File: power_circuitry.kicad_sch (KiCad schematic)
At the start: 32 parts, among them U1 ACS723xLCTR-10AU, U2 ACS723xLCTR-10AU, U3 MCP6007, U4 MCP6007, U5 MCP6007, U6 ACS723xLCTR-10AU, U7 MCP6007, U8 MCP6007, U9 MCP6007

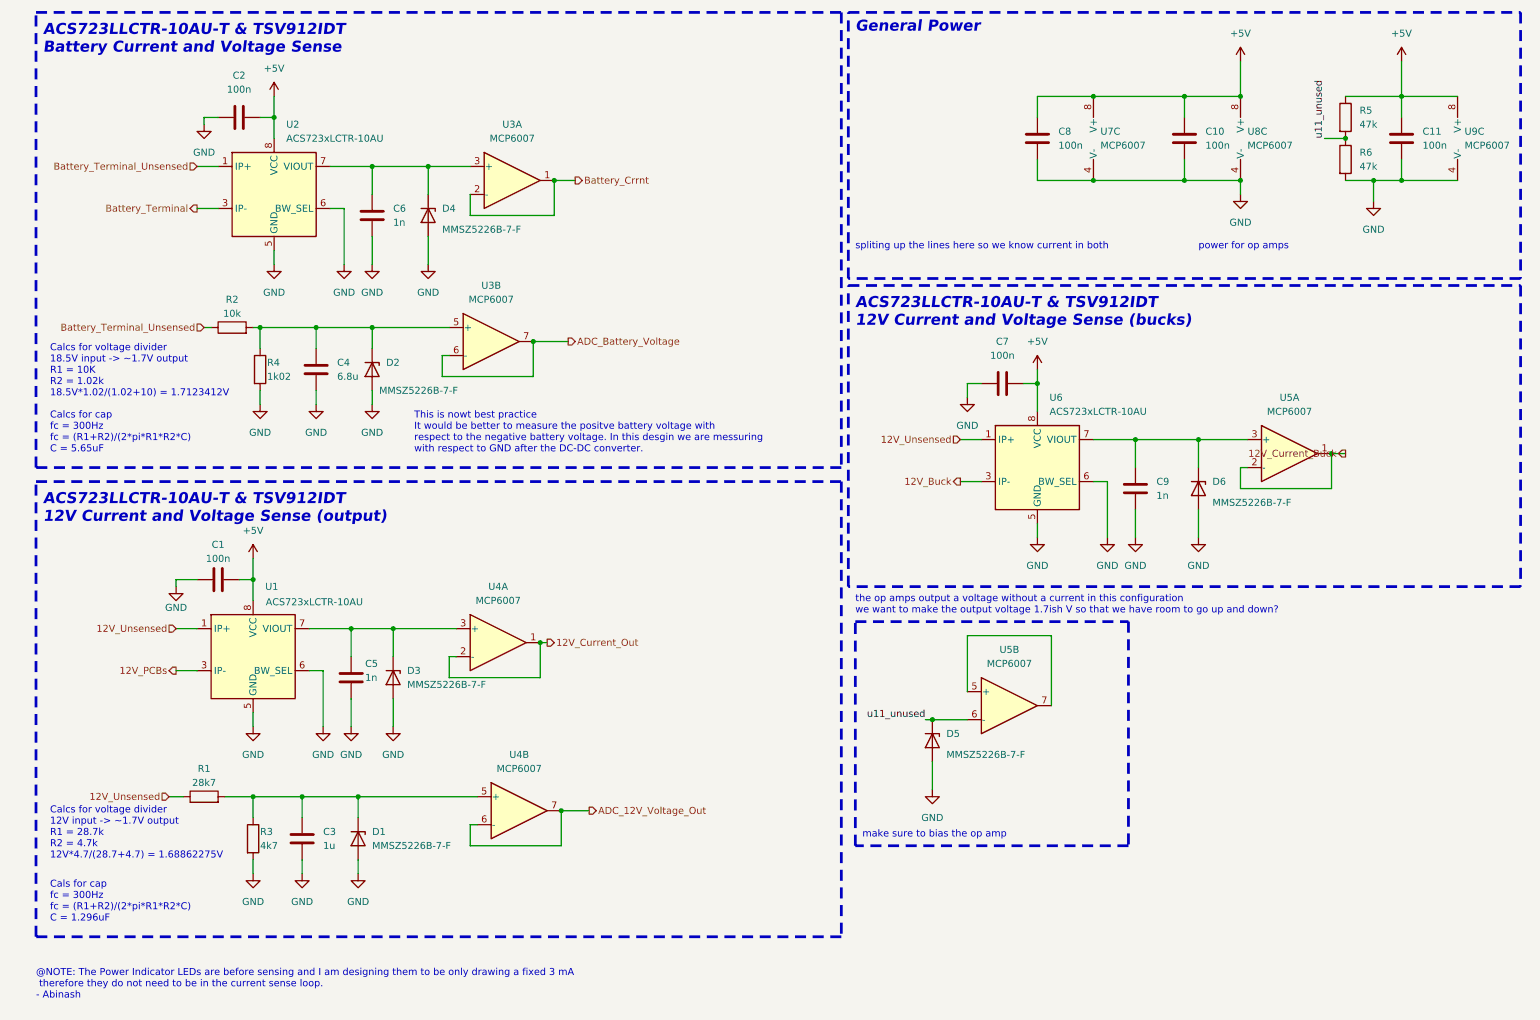
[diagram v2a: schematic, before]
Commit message: transferred correct schematics to rev2
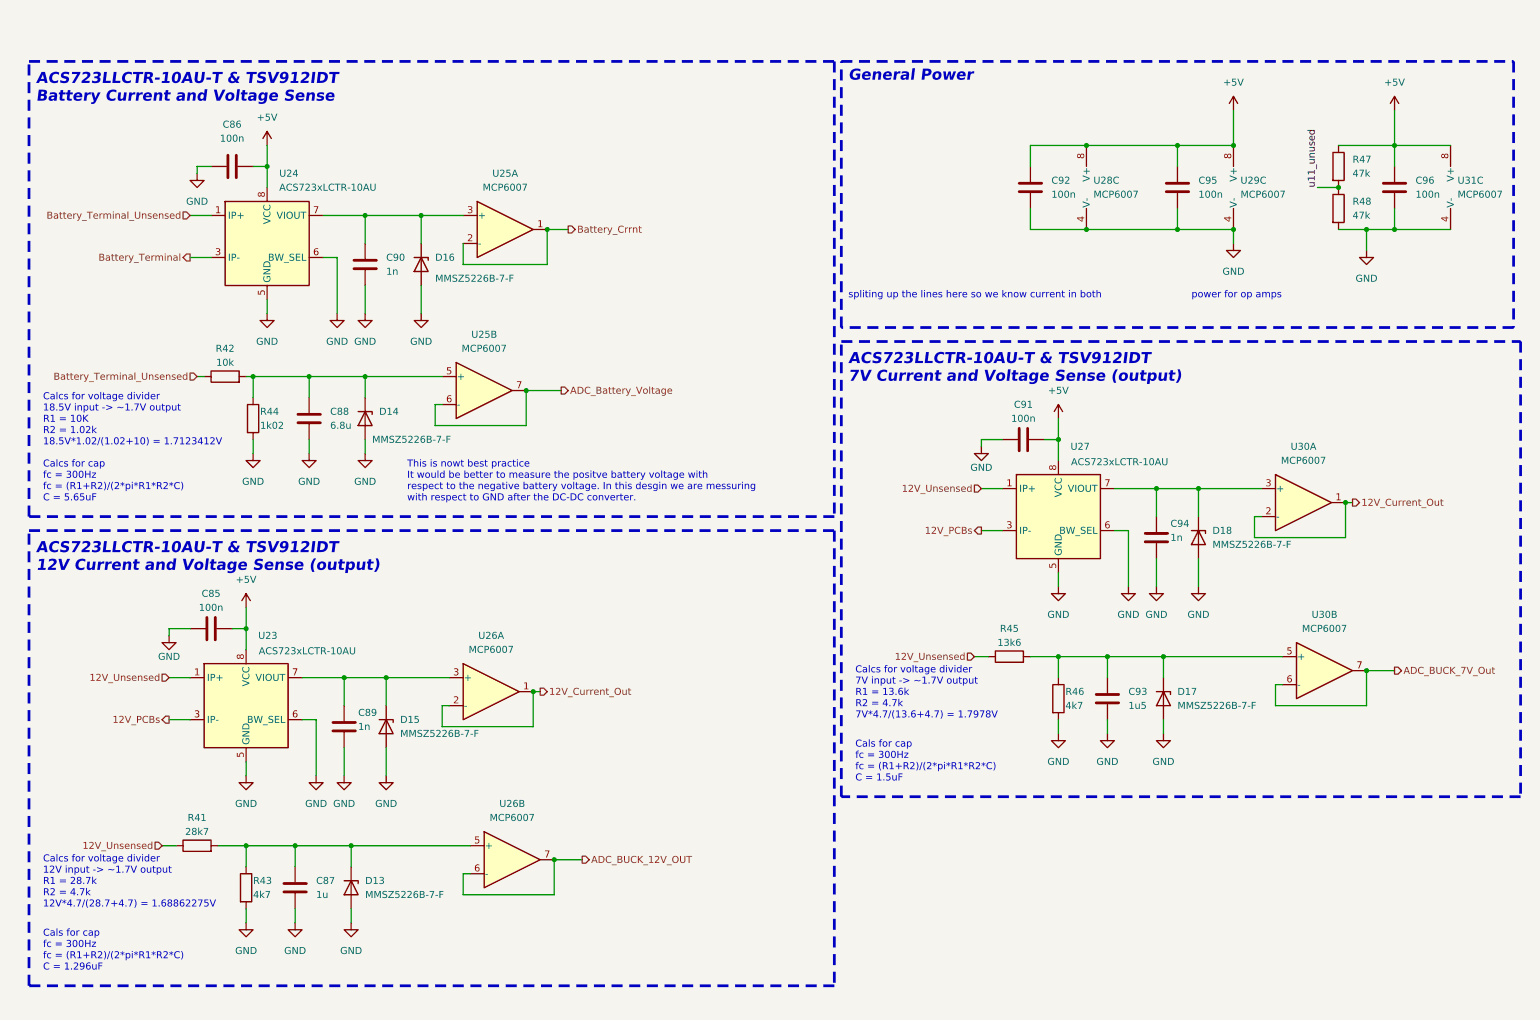
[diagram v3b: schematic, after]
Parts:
- removed C1, C10, C11, C7, C8: 100n, Capacitor_SMD:C_0603_1608Metric, symbol Device:C
- removed C2: 100n, Capacitor_SMD:C_0402_1005Metric, symbol Device:C
- removed C3: 1u, Capacitor_SMD:C_0603_1608Metric, symbol Device:C
- removed C4: 6.8u, Capacitor_SMD:C_0603_1608Metric, symbol Device:C
- removed C5, C6, C9: 1n, Capacitor_SMD:C_0402_1005Metric, symbol Device:C
- removed D1, D2, D3, D4, D5, D6: MMSZ5226B-7-F, Diode_SMD:D_SOD-123, symbol Device:D_Zener
- removed R1: 28k7, Resistor_SMD:R_0603_1608Metric, symbol Device:R
- removed R2: 10k, Resistor_SMD:R_0603_1608Metric, symbol Device:R
- removed R3: 4k7, Resistor_SMD:R_0603_1608Metric, symbol Device:R
- removed R4: 1k02, Resistor_SMD:R_0603_1608Metric, symbol Device:R
- removed R5, R6: 47k, Resistor_SMD:R_0805_2012Metric, symbol Device:R
- removed U1, U2, U6: ACS723xLCTR-10AU, Package_SO:SOIC-8_3.9x4.9mm_P1.27mm, symbol Sensor_Current:ACS723xLCTR-10AU
- removed U3, U4, U5: MCP6007, Package_SO:SOIC-8_3.9x4.9mm_P1.27mm, symbol ecocad_lib_symbols:MCP6007
- removed U7, U8, U9: MCP6007, BP_FTP:SO8_STM, symbol Amplifier_Operational:TSV912IDT
- added C85, C86, C91, C92, C95, C96: 100n, Capacitor_SMD:C_0603_1608Metric, symbol Device:C
- added C87: 1u, Capacitor_SMD:C_0603_1608Metric, symbol Device:C
- added C88: 6.8u, Capacitor_SMD:C_0603_1608Metric, symbol Device:C
- added C89, C90, C94: 1n, Capacitor_SMD:C_0402_1005Metric, symbol Device:C
- added C93: 1u5, Capacitor_SMD:C_0603_1608Metric, symbol Device:C
- added D13, D14, D15, D16, D17, D18: MMSZ5226B-7-F, Diode_SMD:D_SOD-123, symbol Device:D_Zener
- added R41: 28k7, Resistor_SMD:R_0603_1608Metric, symbol Device:R
- added R42: 10k, Resistor_SMD:R_0603_1608Metric, symbol Device:R
- added R43, R46: 4k7, Resistor_SMD:R_0603_1608Metric, symbol Device:R
- added R44: 1k02, Resistor_SMD:R_0603_1608Metric, symbol Device:R
- added R45: 13k6, Resistor_SMD:R_0603_1608Metric, symbol Device:R
- added R47, R48: 47k, Resistor_SMD:R_0805_2012Metric, symbol Device:R
- added U23, U24, U27: ACS723xLCTR-10AU, Package_SO:SOIC-8_3.9x4.9mm_P1.27mm, symbol Sensor_Current:ACS723xLCTR-10AU
- added U25, U26, U30: MCP6007, Package_SO:SOIC-8_3.9x4.9mm_P1.27mm, symbol ecocad_lib_symbols:MCP6007
- added U28, U29, U31: MCP6007, Package_SO:SOIC-8_3.9x4.9mm_P1.27mm, symbol Amplifier_Operational:TSV912IDT
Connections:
- net +5V: now also C85.1, C86.2, C91.1, C92.1, C95.1, C96.1, R47.1, U23.8 (VCC), U24.8 (VCC), U27.8 (VCC), U28.8 (V+), U29.8 (V+), U31.8 (V+)
- net 12V_Current_Out: now also U26.1, U26.2 (-), U30.1, U30.2 (-)
- net 12V_PCBs: now also U23.3 (IP-), U23.4 (IP-), U27.3 (IP-), U27.4 (IP-)
- net 12V_Unsensed: now also R41.1, R45.1, U23.1 (IP+), U23.2 (IP+), U27.1 (IP+), U27.2 (IP+)
- net ADC_Battery_Voltage: now also U25.6 (-), U25.7
- net Battery_Crrnt: now also U25.1, U25.2 (-)
- net Battery_Terminal: now also U24.3 (IP-), U24.4 (IP-)
- net Battery_Terminal_Unsensed: now also R42.1, U24.1 (IP+), U24.2 (IP+)
- net GND: now also C85.2, C86.1, C87.2, C88.2, C89.2, C90.2, C91.2, C92.2, C93.2, C94.2, C95.2, C96.2, D13.2 (A), D14.2 (A), D15.2 (A), D16.2 (A), D17.2 (A), D18.2 (A), R43.2, R44.2, R46.2, R48.2, U23.5 (GND), U23.6 (BW_SEL), U24.5 (GND), U24.6 (BW_SEL), U27.5 (GND), U27.6 (BW_SEL), U28.4 (V-), U29.4 (V-), U31.4 (V-)
- net u11_unused: now also R47.2, R48.1
- new net: C93.1, D17.1 (K), R45.2, R46.1, U30.5 (+)
- new net: C94.1, D18.1 (K), U27.7 (VIOUT), U30.3 (+)
- new net: C90.1, D16.1 (K), U24.7 (VIOUT), U25.3 (+)
- new net: C88.1, D14.1 (K), R42.2, R44.1, U25.5 (+)
- new net: C89.1, D15.1 (K), U23.7 (VIOUT), U26.3 (+)
- new net: C87.1, D13.1 (K), R41.2, R43.1, U26.5 (+)
- new net ADC_BUCK_12V_OUT: U26.6 (-), U26.7
- new net ADC_BUCK_7V_Out: U30.6 (-), U30.7
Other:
- note added: "ACS723LLCTR-10AU-T & TSV912IDT 7V Current and Voltage Sense (output)"
- note added: "Calcs for voltage divider 7V input -> ~1.7V output R1 = 13.6k R2 = 4.7k 7V*4.7/(13.6+4.7) = 1.7978V"
- note added: "Cals for cap fc = 300Hz fc = (R1+R2)/(2*pi*R1*R2*C) C = 1.5uF"
- note removed: "@NOTE: The Power Indicator LEDs are before sensing and I am designing them to be only drawing a fixed 3 mA therefore they do not need to be in the current sense loop. - Abinash"
- note removed: "ACS723LLCTR-10AU-T & TSV912IDT 12V Current and Voltage Sense (bucks)"
- note removed: "make sure to bias the op amp"
- note removed: "the op amps output a voltage without a current in this configuration we want to make the output voltage 1.7ish V so that we have room to go up and down?"

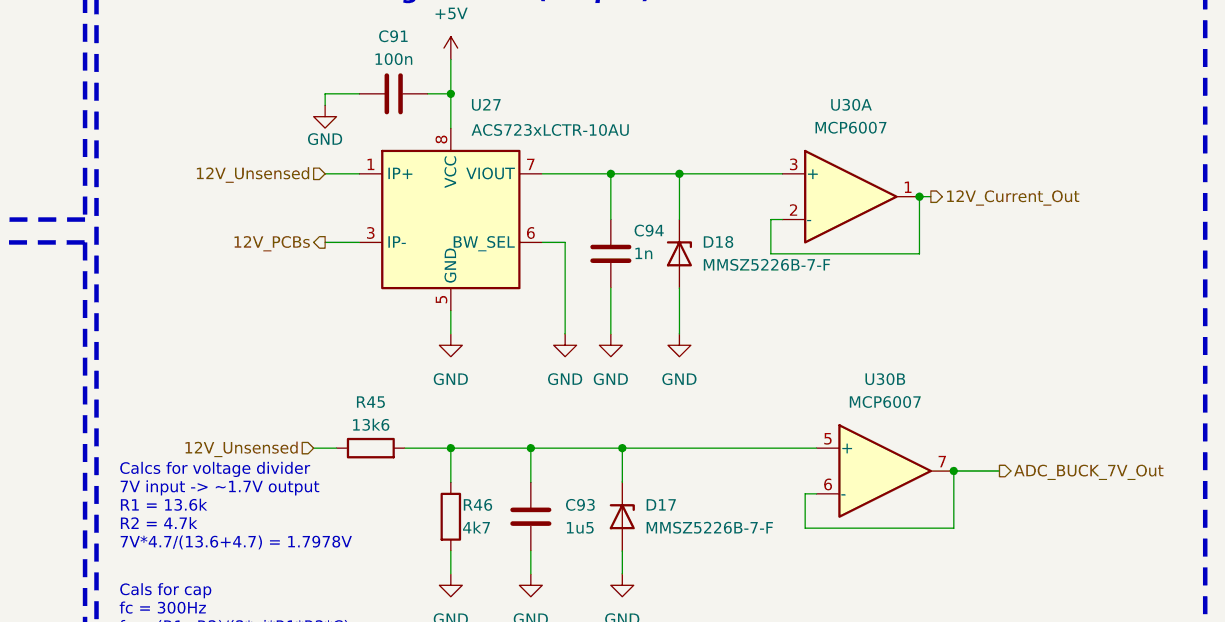
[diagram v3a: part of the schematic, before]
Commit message: Fixed missing symbols and 7V sensor labels
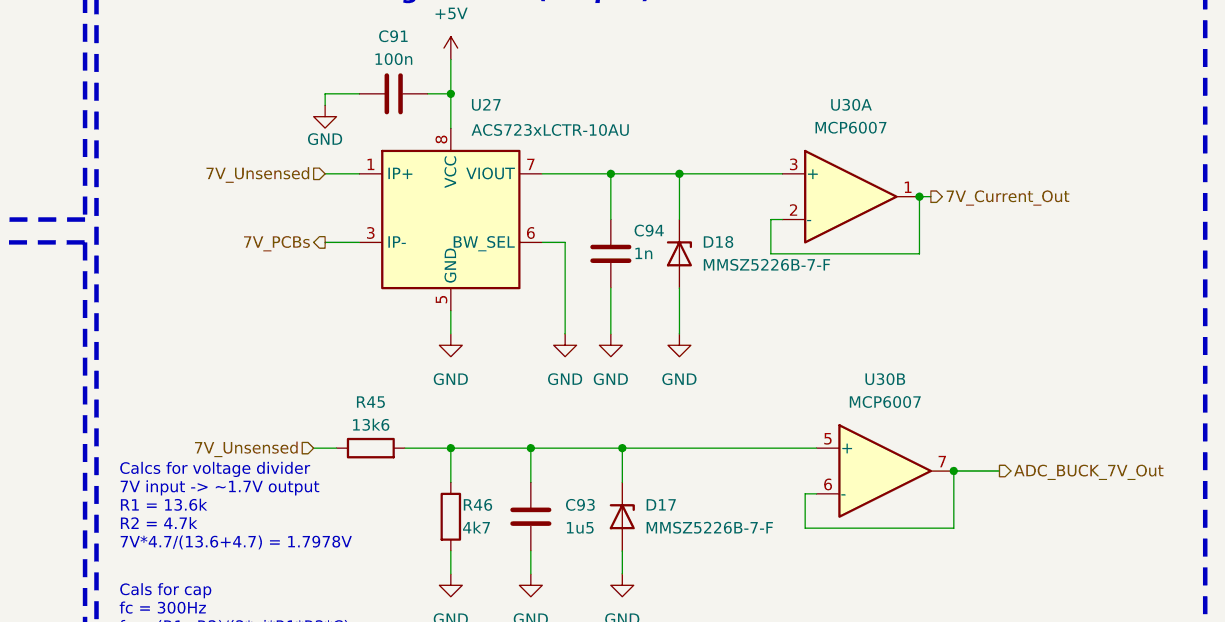
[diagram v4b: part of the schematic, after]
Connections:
- net 12V_Current_Out: no longer U30.1, U30.2 (-)
- net 12V_PCBs: no longer U27.3 (IP-), U27.4 (IP-)
- net 12V_Unsensed: no longer R45.1, U27.1 (IP+), U27.2 (IP+)
- new net 7V_Current_Out: U30.1, U30.2 (-)
- new net 7V_PCBs: U27.3 (IP-), U27.4 (IP-)
- new net 7V_Unsensed: R45.1, U27.1 (IP+), U27.2 (IP+)
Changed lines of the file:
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@@
 		)
 	)
-	(hierarchical_label "12V_Unsensed"
+	(hierarchical_label "7V_Unsensed"
 		(shape input)
 		(at 184.15 129.54 180)
@@
 		)
 	)
-	(hierarchical_label "12V_Unsensed"
+	(hierarchical_label "7V_Unsensed"
 		(shape input)
 		(at 185.42 99.06 180)
@@
 		)
 	)
-	(hierarchical_label "12V_PCBs"
+	(hierarchical_label "7V_PCBs"
 		(shape output)
 		(at 185.42 106.68 180)
@@
 		)
 	)
-	(hierarchical_label "12V_Current_Out"
+	(hierarchical_label "7V_Current_Out"
 		(shape output)
 		(at 252.73 101.6 0)
